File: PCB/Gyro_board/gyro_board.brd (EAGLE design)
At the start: 13 x 10 mm, 5 parts, among them P1 WISP_HEADER, U1 BGM250

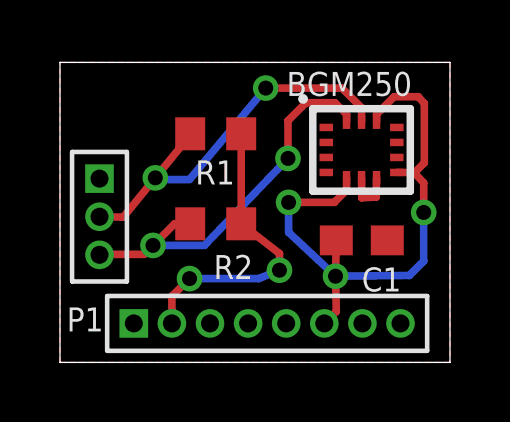
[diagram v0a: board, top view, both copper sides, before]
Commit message: Fix component name typo
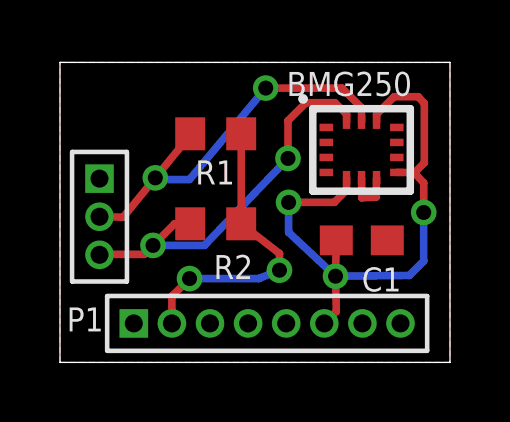
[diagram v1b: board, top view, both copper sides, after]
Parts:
- U1: value BGM250 -> BMG250
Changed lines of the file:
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@@
 <attribute name="NAME" x="0.2248" y="1.0333" size="0.8" layer="25" ratio="10"/>
 </element>
-<element name="U1" library="robot_pcb2" package="LGA14L" value="BGM250" x="10.052" y="7.082" smashed="yes">
+<element name="U1" library="robot_pcb2" package="LGA14L" value="BMG250" x="10.052" y="7.082" smashed="yes">
 <attribute name="VALUE" x="7.552" y="8.882" size="0.8" layer="25" font="vector" ratio="14"/>
 </element>
